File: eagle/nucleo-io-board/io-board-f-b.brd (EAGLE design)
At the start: 100 x 80 mm, 166 parts, among them IC1 LM2574N-5.0, IC2 CAN-TXR-SO8, J1 DCJ0202, P1 9-15V DC, U1 CAN-TXR-PDIP, U10 TC4426/28, U11 74AHCT595N, U13 74AHCT595N, U2 AP1509-50, U3 74HC166, U4 74HC166, U5 TC4426/28, U6 LM324N, U7 TC4426/28, U8 TC4426/28, U9 LM324N, X1 RJ45-JACK, X2 RJ45-JACK, X3 M08-SCREW, X4 M08-SCREW, X6 M08-SCREW, X7 PORTD, X8 PORTE

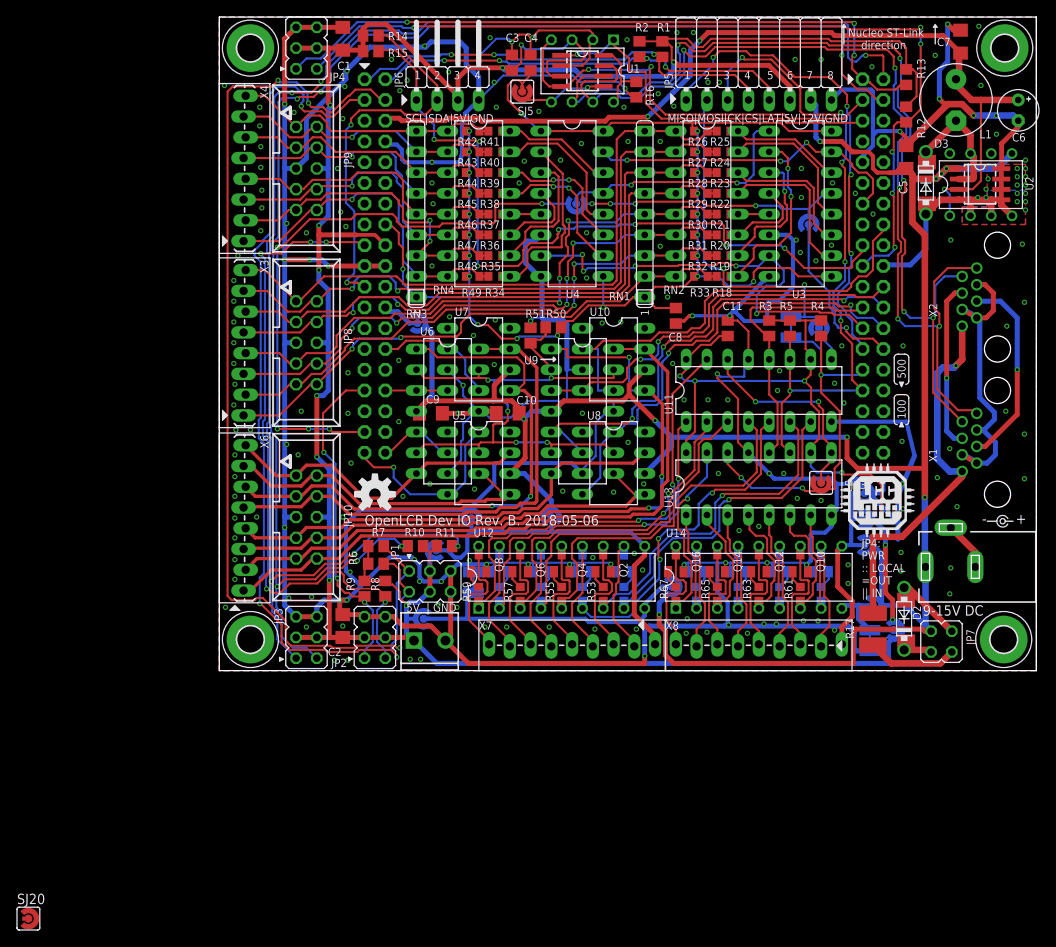
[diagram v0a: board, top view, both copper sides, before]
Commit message: New revisions to fix comments from the review process.
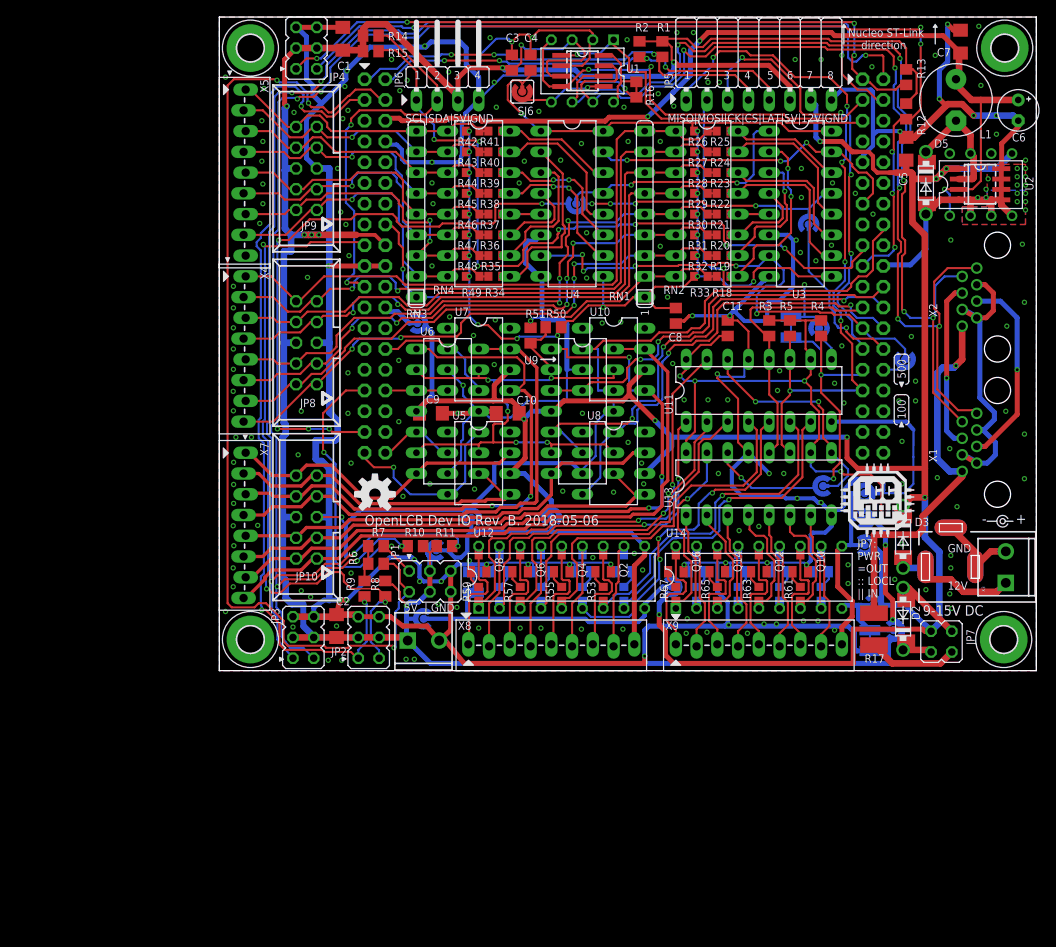
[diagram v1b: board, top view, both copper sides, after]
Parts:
- added D5: (no value), diode:DO41-7.6
- added D6: DIODEDO-214AA-NODOC, trainlib:DO214AA-NODOC
- added X9: PORTE, trainlib:1X09_TERMINAL
- D3: value (none) -> DIODEDO-214AA-NODOC; device diode:DO41-7.6 -> trainlib:DO214AA-NODOC
- D4: value DIODEDO-214AA-NODOC -> (none); device trainlib:DO214AA-NODOC -> diode:DO41-7.6
- J1: device con-jack:DCJ0202 -> trainlib:DCJ0202
- JP10: value (none) -> PORTC
- JP8: value (none) -> PORTB
- JP9: value (none) -> PORTA
- R14, R15: value (none) -> 5k
- SJ11, SJ18, SJ3: device trainlib:SJW-C -> trainlib:SJ_RND2
- SJ12, SJ19, SJ4: device trainlib:SJ_RND2 -> trainlib:SJW-C
- U10, U5, U7, U8: value TC4426/28 -> TC4427
- X3, X6: value M08-SCREW -> (none); device trainlib:1X08_TERMINAL -> SPCoast:SCREWTERMINAL-3.5MM-2_LOCK
- X5: value (none) -> M09-SCREW; device SPCoast:SCREWTERMINAL-3.5MM-2_LOCK -> trainlib:1X09_TERMINAL
- X7: value PORTD -> M08-SCREW; device trainlib:1X09_TERMINAL -> trainlib:1X08_TERMINAL
- X8: value PORTE -> PORTD
- moved SJ20 114.8 mm to (79.0, 21.7), flipped to the bottom, turned to 180 degrees
- moved X3 100.7 mm to (96.3, 10.9), turned to 90 degrees
- moved X5 70.6 mm to (3.10, 71.1), turned to 270 degrees
- moved SJ2 59.9 mm to (83.9, 38.1), turned to 270 degrees
- moved SJ7 54.1 mm to (43.7, 57.1), turned to 270 degrees
- moved SJ5 46.5 mm to (73.4, 41.9), flipped to the bottom, turned to 90 degrees
- moved SJ3 45.7 mm to (24.3, 42.5), turned to 180 degrees
- moved D4 43.4 mm to (83.7, 16.4)
- moved D3 43.4 mm to (83.7, 16.4)
- moved SJ13 43.0 mm to (30.9, 18.7), flipped to the bottom, turned to 90 degrees
- moved X7 38.1 mm to (3.10, 26.7), turned to 270 degrees
- moved X6 31.3 mm to (23.2, 3.68), turned to 0 degrees
- moved SJ9 29.2 mm to (26.5, 14.7), turned to 0 degrees
- moved X8 25.4 mm to (30.5, 3.10)
- moved X4 22.1 mm to (3.10, 48.3)
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- renumbered IC1 to U2B, IC2 to U1B
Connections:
- removed net N$36: JP8.1, R25.2, R26.2, RN1.9, RN2.1, X3.1
- removed net N$54: G1.PB13, SJ20.P$2
- new net N$4: D3.A, D4.A, J1.1, J1.1B, X3.1
- new net N$5: JP8.10, R25.2, R26.2, RN1.9, RN2.1, X4.1
- new net SCK2_ALT: G1.PB13, SJ2.P$2
- net +12V: now also D3.C, D4.C, SJ11.P$2, SJ18.P$2, SJ3.P$2; no longer J1.1, SJ16.P$2, SJ2.P$2, SJ9.P$2
- net +3V3: now also SJ6.P$1; no longer SJ5.P$1
- net +5V: now also SJ16.P$2, SJ9.P$2, X6.1; no longer SJ14.P$2, SJ7.P$2, X5.1
- net CAN_VIO: now also SJ6.P$2; no longer SJ5.P$2
- net E_MOSI: now also SJ4.2, SJ5.P$2; no longer SJ3.2, SJ4.P$2
- net GND: now also D5.A, D6.A, J1.2B, J1.3B, SJ12.2, SJ13.P$2, SJ19.2, SJ20.P$2, X3.2, X5.9, X6.2; no longer D3.A, D4.A, SJ11.2, SJ12.P$2, SJ18.2, SJ19.P$2, X5.2
- net LPOWA: now also SJ10.P$1, SJ12.1, SJ8.P$1; no longer SJ11.1, SJ7.P$1, SJ9.P$1
- net LPOWB: now also SJ11.P$1, SJ13.P$1, SJ9.P$1, X8.9; no longer SJ10.P$1, SJ12.P$1, SJ8.P$1, X7.9
- net MISO2: now also SJ7.P$2; no longer SJ6.P$2
- net MOSI: now also SJ14.P$2, SJ4.1; no longer SJ13.P$2, SJ3.1
- net N$101: now also X8.7; no longer X7.7
- net N$11: now also X9.4; no longer X8.4
- net N$13: now also X9.5; no longer X8.5
- net N$14: now also JP9.2, X5.7; no longer JP9.9, X4.7
- net N$15: now also JP9.3, X5.6; no longer JP9.8, X4.6
- net N$18: now also X9.6; no longer X8.6
- net N$19: now also JP9.7, X5.4; no longer JP9.4, X4.4
- net N$2: now also X9.1; no longer X8.1
- net N$20: now also JP9.8, X5.3; no longer JP9.3, X4.3
- net N$21: now also JP8.3, X4.6; no longer JP8.8, X3.6
- net N$22: now also JP9.10, X5.1; no longer JP9.1, X4.1
- net N$25: now also JP8.1, X4.8; no longer JP8.10, X3.8
- net N$26: now also JP8.2, X4.7; no longer JP8.9, X3.7
- net N$28: now also JP8.4, X4.5; no longer JP8.7, X3.5
- net N$33: now also JP8.7, X4.4; no longer JP8.4, X3.4
- net N$34: now also JP8.8, X4.3; no longer JP8.3, X3.3
- net N$35: now also JP8.9, X4.2; no longer JP8.2, X3.2
- net N$40: now also X9.7; no longer X8.7
- net N$42: now also X9.8; no longer X8.8
- net N$6: now also JP9.1, X5.8; no longer JP9.10, X4.8
- net N$60: now also SJ3.P$1; no longer SJ2.P$1
- net N$7: now also X9.2; no longer X8.2
- net N$75: now also X8.8; no longer X7.8
- net N$83: now also JP9.4, X5.5; no longer JP9.7, X4.5
- net N$84: now also JP9.9, X5.2; no longer JP9.2, X4.2
- net N$87: now also X8.1; no longer X7.1
- net N$9: now also X9.3; no longer X8.3
- net N$91: now also X8.2; no longer X7.2
- net N$93: now also X8.3; no longer X7.3
- net N$95: now also X8.4; no longer X7.4
- net N$97: now also X8.5; no longer X7.5
- net N$99: now also X8.6; no longer X7.6
- net RPOWA: now also SJ15.P$1, SJ17.P$1, SJ19.1; no longer SJ14.P$1, SJ16.P$1, SJ18.1
- net RPOWB: now also SJ16.P$1, SJ18.P$1, SJ20.P$1, X9.9; no longer SJ15.P$1, SJ17.P$1, SJ19.P$1, X8.9
- net SCK2: now also SJ2.P$1; no longer SJ20.P$1
- net SLNK1: now also SJ14.P$1; no longer SJ13.P$1
- net SLNK2: now also SJ5.P$1; no longer SJ4.P$1
- net SLNK3: now also SJ7.P$1; no longer SJ6.P$1
- net SRV5: now also G1.PC12; no longer G1.PF1-PH1
- net SRV7: now also G1.PF1-PH1; no longer G1.PC12
- net SW: now also D5.C, D6.C; no longer D3.C, D4.C
- net TOUT1: now also JP10.10, X7.1; no longer JP10.1, X6.1
- net TOUT2: now also JP10.9, X7.2; no longer JP10.2, X6.2
- net TOUT3: now also JP10.8, X7.3; no longer JP10.3, X6.3
- net TOUT4: now also JP10.7, X7.4; no longer JP10.4, X6.4
- net TOUT5: now also JP10.4, X7.5; no longer JP10.7, X6.5
- net TOUT6: now also JP10.3, X7.6; no longer JP10.8, X6.6
- net TOUT7: now also JP10.2, X7.7; no longer JP10.9, X6.7
- net TOUT8: now also JP10.1, X7.8; no longer JP10.10, X6.8
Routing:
- net N$36: track 79.7 -> 0.00 mm
- net N$5: track 0.00 -> 79.3 mm
- net SRV7: track 116.9 -> 38.5 mm, vias 3 -> 2
- net SRV5: track 40.3 -> 104.1 mm
- net N$4: track 0.00 -> 16.5 mm
- net +5V: track 432.9 -> 441.0 mm, vias 17 -> 15
- net +12V: track 268.7 -> 276.1 mm
- net SCK2: track 55.1 -> 62.5 mm
- net SLNK1: track 25.2 -> 28.2 mm
- net SCK2_ALT: track 0.00 -> 2.77 mm
- net SRV6: track 81.1 -> 82.4 mm, vias 5 -> 3
- net TOUT8: track 80.0 -> 81.1 mm
- net SRV8: track 124.0 -> 125.1 mm
- net N$99: track 14.8 -> 13.7 mm
- net N$93: track 15.7 -> 14.6 mm
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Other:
- board text added: "GND 12V"
- board text added: "JP7: PWR =OUT :: LOCL || IN"
- board text removed: "JP4: PWR :: LOCAL =OUT || IN"
